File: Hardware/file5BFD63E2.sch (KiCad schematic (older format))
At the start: 8 parts, among them J18 Power_Connector_IO, J20 Digital_Connector_IO, J21 CV_Connector_IO, J22 Pot_Connector_IO, J23 Attenuverter_Connector_IO, J28 SID_Audio_Connector_IO

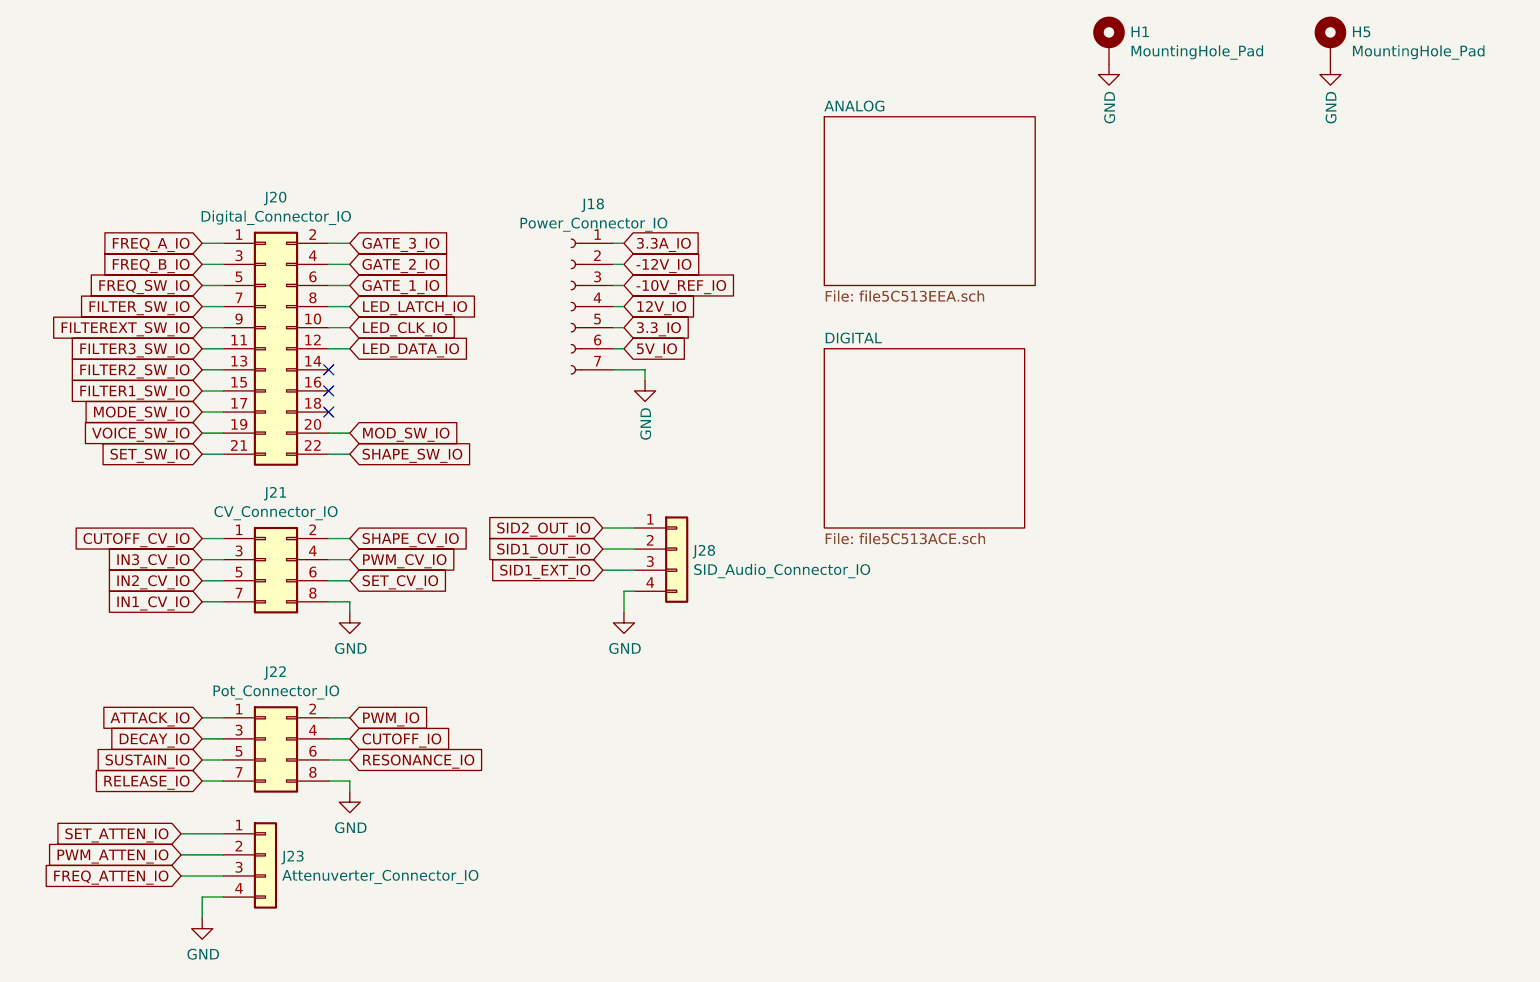
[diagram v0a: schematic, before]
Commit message: Updated to single four layer board
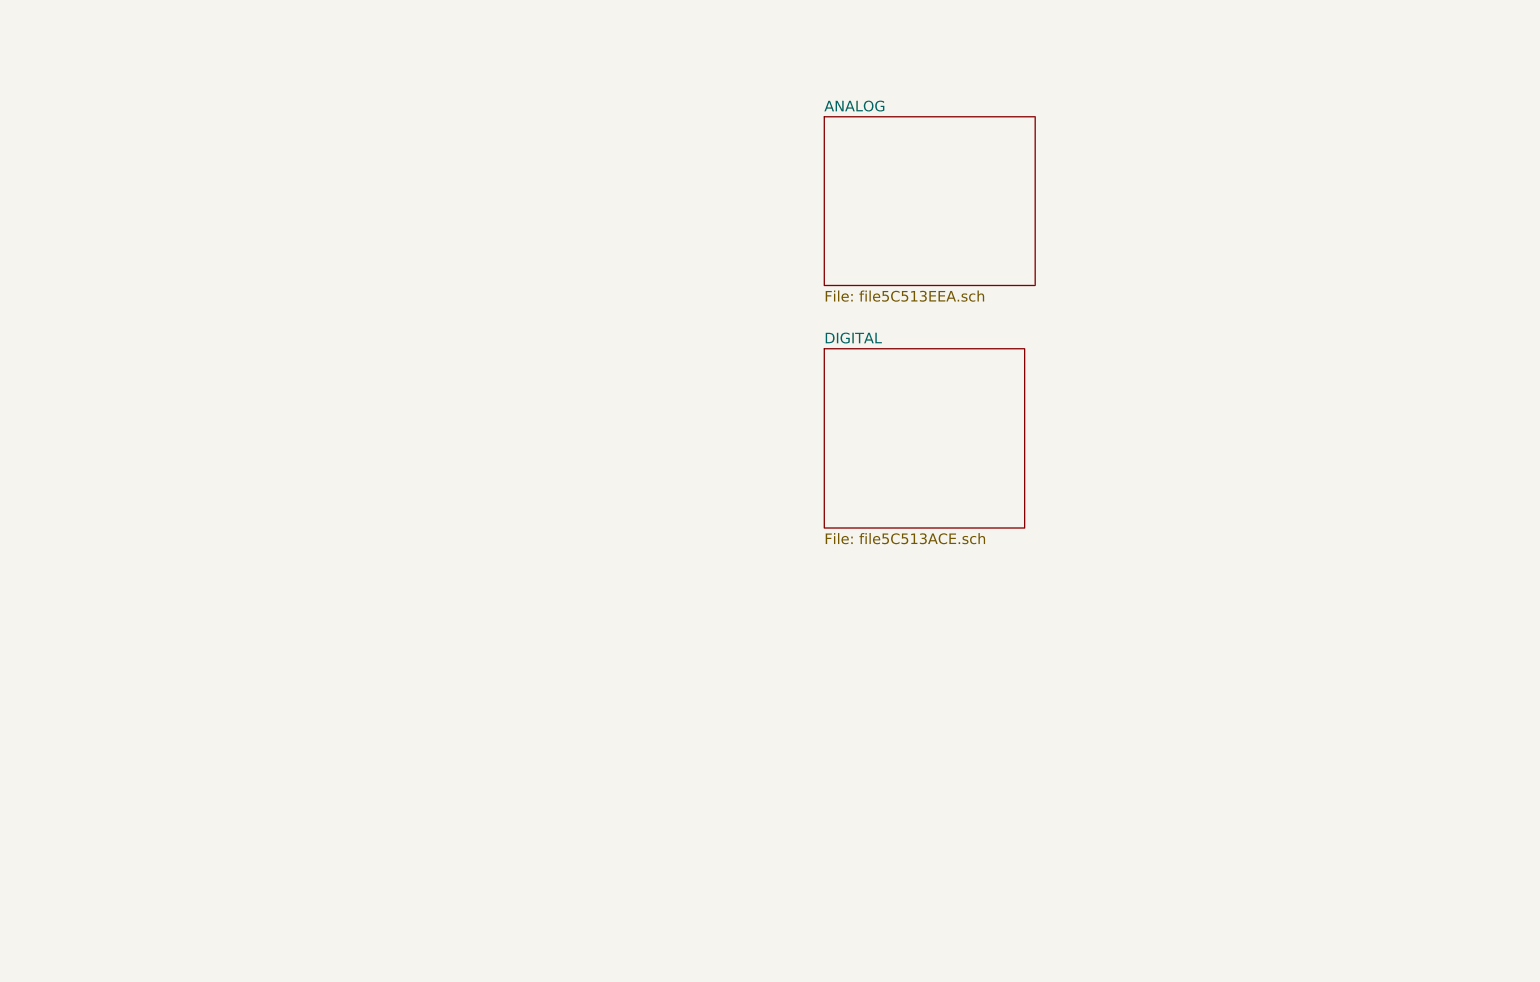
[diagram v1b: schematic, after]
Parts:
- removed H1, H5: MountingHole_Pad, MountingHole:MountingHole_3.2mm_M3_DIN965_Pad, symbol Mechanical:MountingHole_Pad
- removed J18: Power_Connector_IO, Connector_PinSocket_2.54mm:PinSocket_1x07_P2.54mm_Vertical, symbol Connector:Conn_01x07_Female
- removed J20: Digital_Connector_IO, Connector_PinSocket_2.54mm:PinSocket_2x11_P2.54mm_Vertical_SMD, symbol Connector_Generic:Conn_02x11_Odd_Even
- removed J21: CV_Connector_IO, Connector_PinSocket_2.54mm:PinSocket_2x04_P2.54mm_Vertical, symbol Connector_Generic:Conn_02x04_Odd_Even
- removed J22: Pot_Connector_IO, Connector_PinSocket_2.54mm:PinSocket_2x04_P2.54mm_Vertical, symbol Connector_Generic:Conn_02x04_Odd_Even
- removed J23: Attenuverter_Connector_IO, Connector_PinSocket_2.54mm:PinSocket_1x04_P2.54mm_Vertical, symbol Connector_Generic:Conn_01x04
- removed J28: SID_Audio_Connector_IO, Connector_PinSocket_2.54mm:PinSocket_1x04_P2.54mm_Vertical, symbol Connector_Generic:Conn_01x04
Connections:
- no-connect marks 3 -> 0

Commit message: Seperated two board with headers
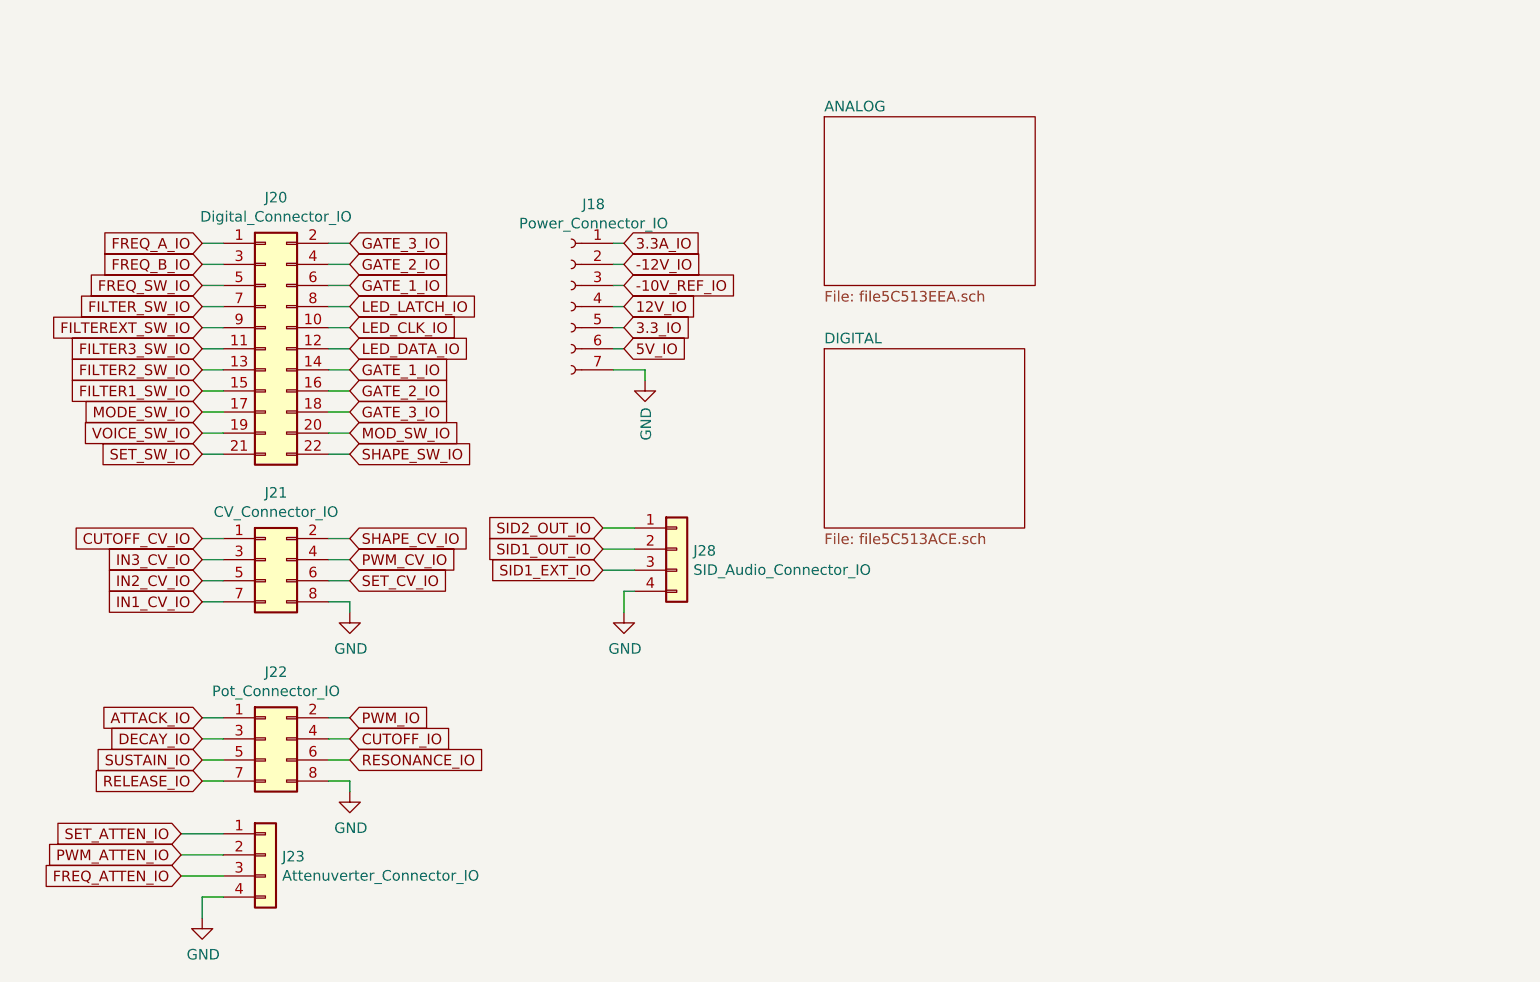
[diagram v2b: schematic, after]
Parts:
- added J18: Power_Connector_IO, Connector_PinSocket_2.54mm:PinSocket_1x07_P2.54mm_Vertical_SMD_Pin1Left, symbol Connector:Conn_01x07_Female
- added J20: Digital_Connector_IO, Connector_PinSocket_2.54mm:PinSocket_2x11_P2.54mm_Vertical_SMD, symbol Connector_Generic:Conn_02x11_Odd_Even
- added J21: CV_Connector_IO, Connector_PinSocket_2.54mm:PinSocket_2x04_P2.54mm_Vertical_SMD, symbol Connector_Generic:Conn_02x04_Odd_Even
- added J22: Pot_Connector_IO, Connector_PinSocket_2.54mm:PinSocket_2x04_P2.54mm_Vertical_SMD, symbol Connector_Generic:Conn_02x04_Odd_Even
- added J23: Attenuverter_Connector_IO, Connector_PinSocket_2.54mm:PinSocket_1x04_P2.54mm_Vertical_SMD_Pin1Left, symbol Connector_Generic:Conn_01x04
- added J28: SID_Audio_Connector_IO, Connector_PinSocket_2.54mm:PinSocket_1x04_P2.54mm_Vertical_SMD_Pin1Left, symbol Connector_Generic:Conn_01x04
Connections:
- new net -10V_REF_IO: J18.3 (Pin_3)
- new net -12V_IO: J18.2 (Pin_2)
- new net 12V_IO: J18.4 (Pin_4)
- new net 3.3A_IO: J18.1 (Pin_1)
- new net 3.3_IO: J18.5 (Pin_5)
- new net 5V_IO: J18.6 (Pin_6)
- new net ATTACK_IO: J22.1 (Pin_1)
- new net CUTOFF_CV_IO: J21.1 (Pin_1)
- new net CUTOFF_IO: J22.4 (Pin_4)
- new net DECAY_IO: J22.3 (Pin_3)
- new net FILTER1_SW_IO: J20.15 (Pin_15)
- new net FILTER2_SW_IO: J20.13 (Pin_13)
- new net FILTER3_SW_IO: J20.11 (Pin_11)
- new net FILTEREXT_SW_IO: J20.9 (Pin_9)
- new net FILTER_SW_IO: J20.7 (Pin_7)
- new net FREQ_ATTEN_IO: J23.3 (Pin_3)
- new net FREQ_A_IO: J20.1 (Pin_1)
- new net FREQ_B_IO: J20.3 (Pin_3)
- new net FREQ_SW_IO: J20.5 (Pin_5)
- new net GATE_1_IO: J20.14 (Pin_14), J20.6 (Pin_6)
- new net GATE_2_IO: J20.16 (Pin_16), J20.4 (Pin_4)
- new net GATE_3_IO: J20.18 (Pin_18), J20.2 (Pin_2)
- new net GND: J18.7 (Pin_7), J21.8 (Pin_8), J22.8 (Pin_8), J23.4 (Pin_4), J28.4 (Pin_4)
- new net IN1_CV_IO: J21.7 (Pin_7)
- new net IN2_CV_IO: J21.5 (Pin_5)
- new net IN3_CV_IO: J21.3 (Pin_3)
- new net LED_CLK_IO: J20.10 (Pin_10)
- new net LED_DATA_IO: J20.12 (Pin_12)
- new net LED_LATCH_IO: J20.8 (Pin_8)
- new net MODE_SW_IO: J20.17 (Pin_17)
- new net MOD_SW_IO: J20.20 (Pin_20)
- new net PWM_ATTEN_IO: J23.2 (Pin_2)
- new net PWM_CV_IO: J21.4 (Pin_4)
- new net PWM_IO: J22.2 (Pin_2)
- new net RELEASE_IO: J22.7 (Pin_7)
- new net RESONANCE_IO: J22.6 (Pin_6)
- new net SET_ATTEN_IO: J23.1 (Pin_1)
- new net SET_CV_IO: J21.6 (Pin_6)
- new net SET_SW_IO: J20.21 (Pin_21)
- new net SHAPE_CV_IO: J21.2 (Pin_2)
- new net SHAPE_SW_IO: J20.22 (Pin_22)
- new net SID1_EXT_IO: J28.3 (Pin_3)
- new net SID1_OUT_IO: J28.2 (Pin_2)
- new net SID2_OUT_IO: J28.1 (Pin_1)
- new net SUSTAIN_IO: J22.5 (Pin_5)
- new net VOICE_SW_IO: J20.19 (Pin_19)

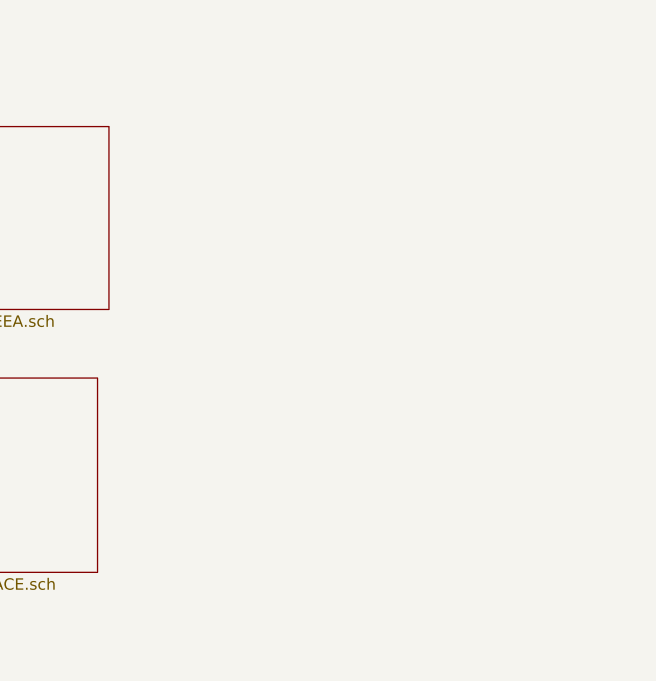
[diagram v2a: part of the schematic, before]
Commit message: Added standof holes
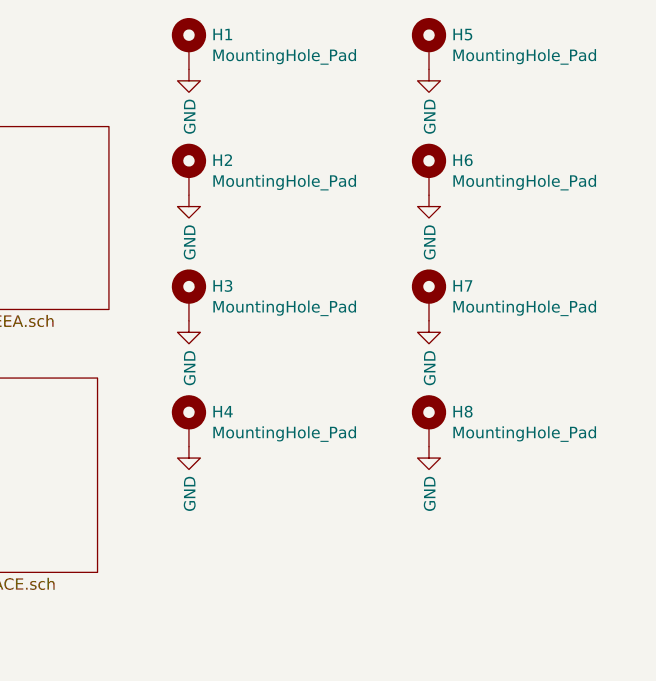
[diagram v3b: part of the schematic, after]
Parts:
- added H1, H2, H3, H4, H5, H6, H7, H8: MountingHole_Pad, MountingHole:MountingHole_3.2mm_M3_DIN965_Pad, symbol Mechanical:MountingHole_Pad
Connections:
- net GND: now also H1.1, H2.1, H3.1, H4.1, H5.1, H6.1, H7.1, H8.1
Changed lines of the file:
@@
 Wire Wire Line
 	3650 4650 3800 4650
+$Comp
+L Mechanical:MountingHole_Pad H5
+U 1 1 5BE3756F
+P 7100 2350
+F 0 "H5" H 7200 2401 50  0000 L CNN
+F 1 "MountingHole_Pad" H 7200 2310 50  0000 L CNN
+F 2 "MountingHole:MountingHole_3.2mm_M3_DIN965_Pad" H 7100 2350 50  0001 C CNN
+F 3 "~" H 7100 2350 50  0001 C CNN
+	1    7100 2350
+	1    0    0    -1
+$EndComp
+$Comp
+L Mechanical:MountingHole_Pad H6
+U 1 1 5BE3763A
+P 7100 2900
+F 0 "H6" H 7200 2951 50  0000 L CNN
+F 1 "MountingHole_Pad" H 7200 2860 50  0000 L CNN
+F 2 "MountingHole:MountingHole_3.2mm_M3_DIN965_Pad" H 7100 2900 50  0001 C CNN
+F 3 "~" H 7100 2900 50  0001 C CNN
+	1    7100 2900
+	1    0    0    -1
+$EndComp
+$Comp
+L Mechanical:MountingHole_Pad H7
+U 1 1 5BE3766D
+P 7100 3450
+F 0 "H7" H 7200 3501 50  0000 L CNN
+F 1 "MountingHole_Pad" H 7200 3410 50  0000 L CNN
+F 2 "MountingHole:MountingHole_3.2mm_M3_DIN965_Pad" H 7100 3450 50  0001 C CNN
+F 3 "~" H 7100 3450 50  0001 C CNN
+	1    7100 3450
+	1    0    0    -1
+$EndComp
+$Comp
+L Mechanical:MountingHole_Pad H8
+U 1 1 5BE376A0
+P 7100 4000
+F 0 "H8" H 7200 4051 50  0000 L CNN
+F 1 "MountingHole_Pad" H 7200 3960 50  0000 L CNN
+F 2 "MountingHole:MountingHole_3.2mm_M3_DIN965_Pad" H 7100 4000 50  0001 C CNN
+F 3 "~" H 7100 4000 50  0001 C CNN
+	1    7100 4000
+	1    0    0    -1
+$EndComp
+$Comp
+L Mechanical:MountingHole_Pad H1
+U 1 1 5BE3F331
+P 6050 2350
+F 0 "H1" H 6150 2401 50  0000 L CNN
+F 1 "MountingHole_Pad" H 6150 2310 50  0000 L CNN
+F 2 "MountingHole:MountingHole_3.2mm_M3_DIN965_Pad" H 6050 2350 50  0001 C CNN
+F 3 "~" H 6050 2350 50  0001 C CNN
+	1    6050 2350
+	1    0    0    -1
+$EndComp
+$Comp
+L Mechanical:MountingHole_Pad H2
+U 1 1 5BE3F338
+P 6050 2900
+F 0 "H2" H 6150 2951 50  0000 L CNN
+F 1 "MountingHole_Pad" H 6150 2860 50  0000 L CNN
+F 2 "MountingHole:MountingHole_3.2mm_M3_DIN965_Pad" H 6050 2900 50  0001 C CNN
+F 3 "~" H 6050 2900 50  0001 C CNN
+	1    6050 2900
+	1    0    0    -1
+$EndComp
+$Comp
+L Mechanical:MountingHole_Pad H3
+U 1 1 5BE3F33F
+P 6050 3450
+F 0 "H3" H 6150 3501 50  0000 L CNN
+F 1 "MountingHole_Pad" H 6150 3410 50  0000 L CNN
+F 2 "MountingHole:MountingHole_3.2mm_M3_DIN965_Pad" H 6050 3450 50  0001 C CNN
+F 3 "~" H 6050 3450 50  0001 C CNN
+	1    6050 3450
+	1    0    0    -1
+$EndComp
+$Comp
+L Mechanical:MountingHole_Pad H4
+U 1 1 5BE3F346
+P 6050 4000
+F 0 "H4" H 6150 4051 50  0000 L CNN
+F 1 "MountingHole_Pad" H 6150 3960 50  0000 L CNN
+F 2 "MountingHole:MountingHole_3.2mm_M3_DIN965_Pad" H 6050 4000 50  0001 C CNN
+F 3 "~" H 6050 4000 50  0001 C CNN
+	1    6050 4000
+	1    0    0    -1
+$EndComp
+$Comp
+L power:GND #PWR?
+U 1 1 5BE41CB1
+P 6050 4100
+AR Path="/5C5B0291/5BE41CB1" Ref="#PWR?"  Part="1"
+AR Path="/5BFD63E3/5BE41CB1" Ref="#PWR?"  Part="1"
+F 0 "#PWR?" H 6050 3850 50  0001 C CNN
+F 1 "GND" V 6055 3972 50  0000 R CNN
+F 2 "" H 6050 4100 50  0001 C CNN
+F 3 "" H 6050 4100 50  0001 C CNN
+	1    6050 4100
+	1    0    0    -1
+$EndComp
+$Comp
+L power:GND #PWR?
+U 1 1 5BE41D02
+P 7100 4100
+AR Path="/5C5B0291/5BE41D02" Ref="#PWR?"  Part="1"
+AR Path="/5BFD63E3/5BE41D02" Ref="#PWR?"  Part="1"
+F 0 "#PWR?" H 7100 3850 50  0001 C CNN
+F 1 "GND" V 7105 3972 50  0000 R CNN
+F 2 "" H 7100 4100 50  0001 C CNN
+F 3 "" H 7100 4100 50  0001 C CNN
+	1    7100 4100
+	1    0    0    -1
+$EndComp
+$Comp
+L power:GND #PWR?
+U 1 1 5BE435B9
+P 6050 3000
+AR Path="/5C5B0291/5BE435B9" Ref="#PWR?"  Part="1"
+AR Path="/5BFD63E3/5BE435B9" Ref="#PWR?"  Part="1"
+F 0 "#PWR?" H 6050 2750 50  0001 C CNN
+F 1 "GND" V 6055 2872 50  0000 R CNN
+F 2 "" H 6050 3000 50  0001 C CNN
+F 3 "" H 6050 3000 50  0001 C CNN
+	1    6050 3000
+	1    0    0    -1
+$EndComp
+$Comp
+L power:GND #PWR?
+U 1 1 5BE435E0
+P 7100 3000
+AR Path="/5C5B0291/5BE435E0" Ref="#PWR?"  Part="1"
+AR Path="/5BFD63E3/5BE435E0" Ref="#PWR?"  Part="1"
+F 0 "#PWR?" H 7100 2750 50  0001 C CNN
+F 1 "GND" V 7105 2872 50  0000 R CNN
+F 2 "" H 7100 3000 50  0001 C CNN
+F 3 "" H 7100 3000 50  0001 C CNN
+	1    7100 3000
+	1    0    0    -1
+$EndComp
+$Comp
+L power:GND #PWR?
+U 1 1 5BE49823
+P 6050 3550
+AR Path="/5C5B0291/5BE49823" Ref="#PWR?"  Part="1"
+AR Path="/5BFD63E3/5BE49823" Ref="#PWR?"  Part="1"
+F 0 "#PWR?" H 6050 3300 50  0001 C CNN
+F 1 "GND" V 6055 3422 50  0000 R CNN
+F 2 "" H 6050 3550 50  0001 C CNN
+F 3 "" H 6050 3550 50  0001 C CNN
+	1    6050 3550
+	1    0    0    -1
+$EndComp
+$Comp
+L power:GND #PWR?
+U 1 1 5BE4984A
+P 7100 3550
+AR Path="/5C5B0291/5BE4984A" Ref="#PWR?"  Part="1"
+AR Path="/5BFD63E3/5BE4984A" Ref="#PWR?"  Part="1"
+F 0 "#PWR?" H 7100 3300 50  0001 C CNN
+F 1 "GND" V 7105 3422 50  0000 R CNN
+F 2 "" H 7100 3550 50  0001 C CNN
+F 3 "" H 7100 3550 50  0001 C CNN
+	1    7100 3550
+	1    0    0    -1
+$EndComp
+$Comp
+L power:GND #PWR?
+U 1 1 5BE49871
+P 6050 2450
+AR Path="/5C5B0291/5BE49871" Ref="#PWR?"  Part="1"
+AR Path="/5BFD63E3/5BE49871" Ref="#PWR?"  Part="1"
+F 0 "#PWR?" H 6050 2200 50  0001 C CNN
+F 1 "GND" V 6055 2322 50  0000 R CNN
+F 2 "" H 6050 2450 50  0001 C CNN
+F 3 "" H 6050 2450 50  0001 C CNN
+	1    6050 2450
+	1    0    0    -1
+$EndComp
+$Comp
+L power:GND #PWR?
+U 1 1 5BE49898
+P 7100 2450
+AR Path="/5C5B0291/5BE49898" Ref="#PWR?"  Part="1"
+AR Path="/5BFD63E3/5BE49898" Ref="#PWR?"  Part="1"
+F 0 "#PWR?" H 7100 2200 50  0001 C CNN
+F 1 "GND" V 7105 2322 50  0000 R CNN
+F 2 "" H 7100 2450 50  0001 C CNN
+F 3 "" H 7100 2450 50  0001 C CNN
+	1    7100 2450
+	1    0    0    -1
+$EndComp
 $EndSCHEMATC
